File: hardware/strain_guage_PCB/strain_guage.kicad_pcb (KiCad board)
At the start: 4 copper layers, 132.7 x 89.5 mm, 97 parts, among them IC1 STM32C091CBT6, J2 Conn_02x05_Odd_Even, J3 Screw_Terminal_01x03, SW1 SW_Push, U1 MCP3561-E/ST, U10 MCP2221A-I/SL, U11 LM2664M6X/NOPB, U2 OP177GPZ, U3 OP177GPZ, U4 OP177GPZ, U5 AD630ARZ, U6 OPA2187IDR, U7 OP177GPZ, U8 AD9833BRMZ, U9 MIC5365-3.3YC5-TR

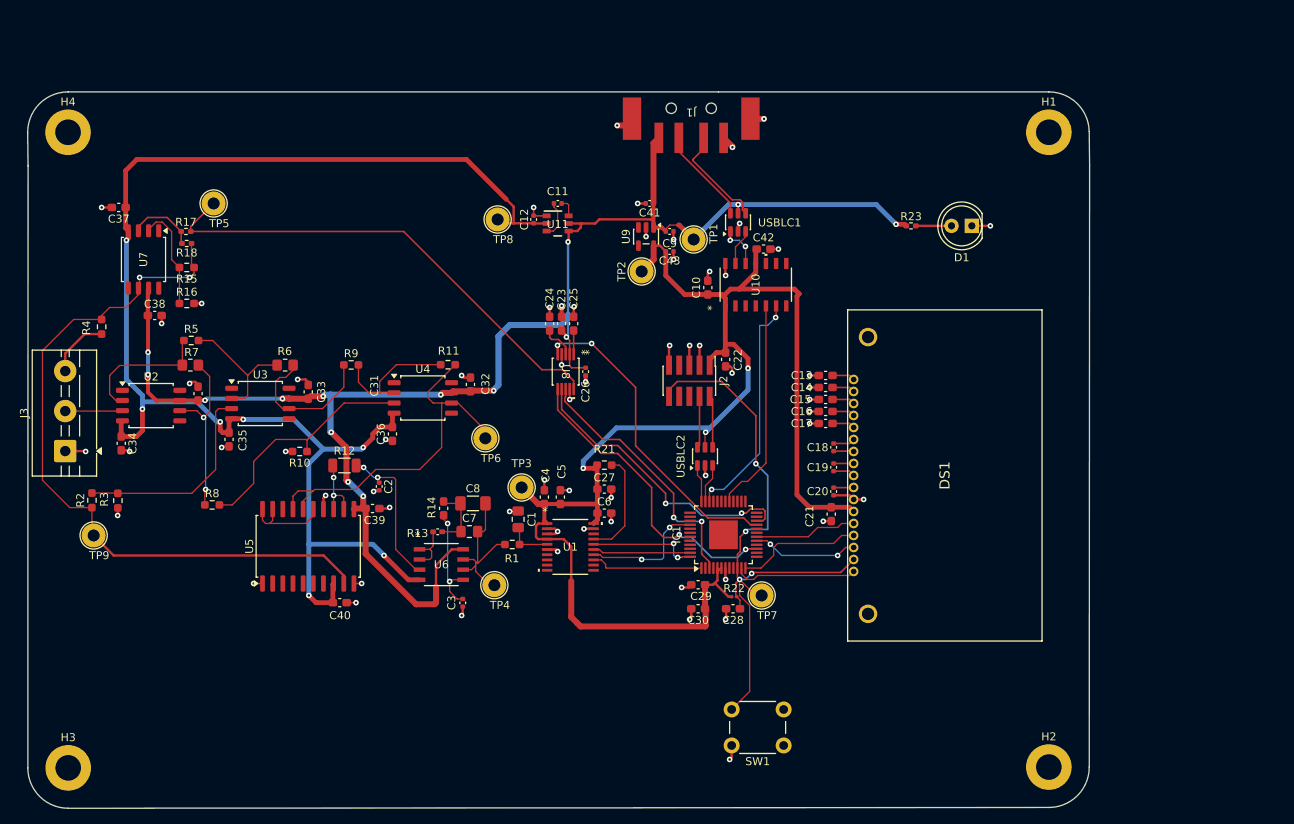
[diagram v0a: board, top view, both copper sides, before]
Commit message: PCB Revision + BOM Update
Footprints for Op-Amps were corrected, package size for R22 was updated. PCB Layout and Tracing marginally modified
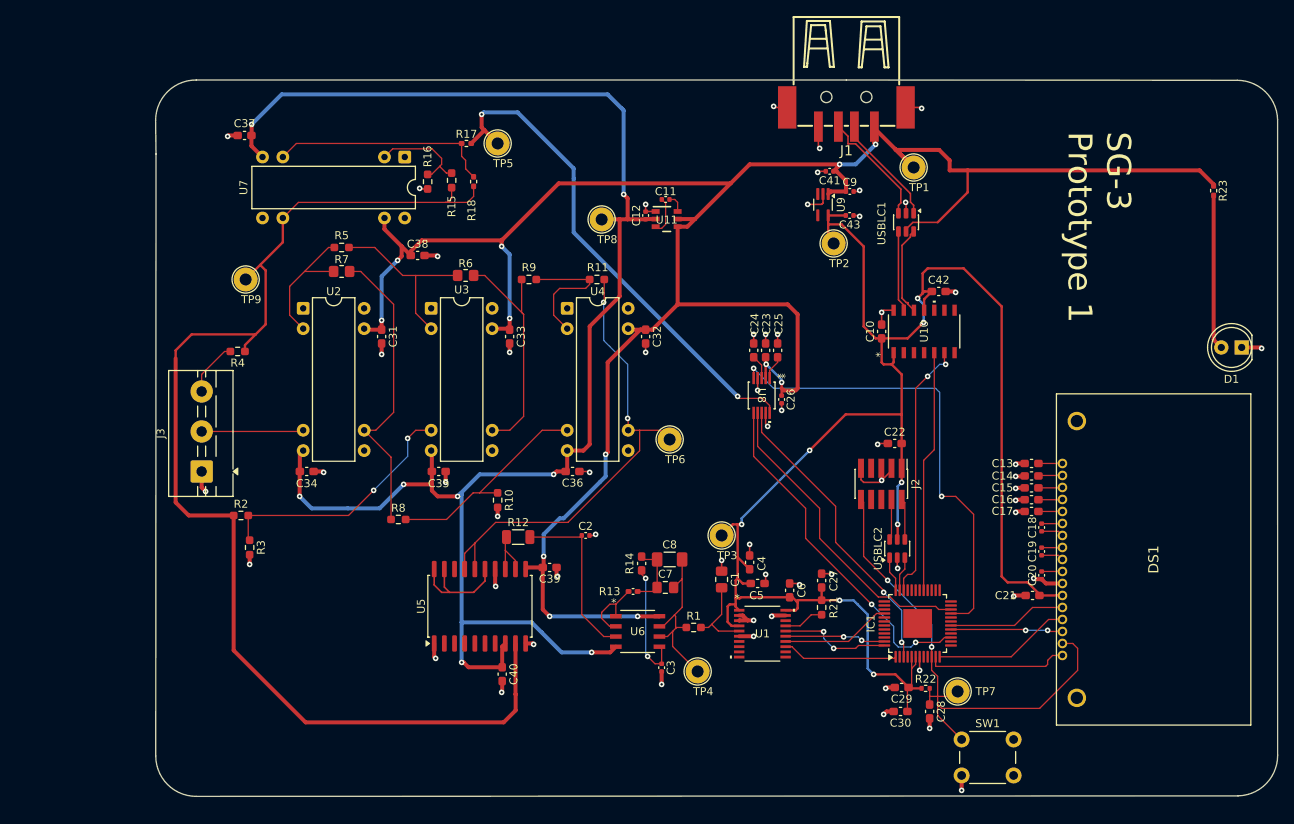
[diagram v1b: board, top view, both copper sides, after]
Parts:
- removed H1, H2, H3, H4: MountingHole_Pad, MountingHole:MountingHole_3.2mm_M3_ISO7380_Pad
- J1: footprint USBC:BX-TYPE-A-MWT4P -> USBC:USB-A-SMD_BX-TYPE-A-MWT4P
- R22: footprint Resistor_SMD:R_0201_0603Metric -> Resistor_SMD:R_0402_1005Metric
- U2, U3, U4, U7: footprint Package_SO:SOIC-8_5.3x5.3mm_P1.27mm -> Package_DIP:DIP-8-16_W7.62mm
- U9: footprint Package_TO_SOT_SMD:TSOT-23-5 -> Package_TO_SOT_SMD:SOT-353_SC-70-5_Handsoldering
- moved R23 38.1 mm to (214.5, 64.9), turned to -90 degrees
- moved TP9 37.2 mm to (93.5, 76.0)
- moved D1 37.0 mm to (218.0, 84.5)
- moved R17 36.7 mm to (121.1, 59.0)
- moved R18 36.7 mm to (122.0, 63.8), turned to 90 degrees
- moved TP5 36.3 mm to (125.0, 59.0)
- moved U7 35.1 mm to (113.4, 60.7)
- moved R15 34.9 mm to (119.2, 63.6), turned to 90 degrees
- moved R16 33.7 mm to (116.2, 63.8), turned to -90 degrees
- moved C38 33.7 mm to (115.0, 73.0)
- moved R21 32.5 mm to (165.5, 117.0), turned to 90 degrees
- moved C27 29.5 mm to (165.5, 113.6), turned to 90 degrees
- moved SW1 29.0 mm to (189.5, 138.0)
- moved TP1 28.9 mm to (177.0, 62.0), turned to 0 degrees
- moved C29 28.5 mm to (175.5, 127.0)
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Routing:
- net +5V: track 201.3 -> 293.8 mm, vias 14 -> 12
- net /C_EXC: track 90.0 -> 152.9 mm, vias 2 -> 0
- net +3V3: track 180.0 -> 218.2 mm, vias 3 -> 8
- net -5V: track 178.8 -> 208.0 mm, vias 7 -> 8
- net Net-(R17-Pad1): track 8.60 -> 27.8 mm
- net /FG_MCLK: track 39.8 -> 58.7 mm
- net Net-(R7-Pad1): track 21.8 -> 37.9 mm, vias 2 -> 0
- net Net-(D1-A): track 4.46 -> 19.4 mm
- net /ina_out: track 46.5 -> 60.8 mm, vias 0 -> 2
- net /NRST: track 78.7 -> 65.6 mm, vias 4 -> 2
- net Net-(R6-Pad1): track 18.7 -> 30.1 mm
- net Net-(U1-*IRQ/MDAT): track 13.4 -> 5.07 mm
- net /USBD-: track 17.6 -> 25.1 mm, vias 2 -> 0
- net /USBD+: track 18.5 -> 24.9 mm
- net Net-(R5-Pad1): track 16.8 -> 22.5 mm
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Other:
- board size 132.7 x 89.5 mm -> 140.3 x 89.5 mm
- board text added: "SG-3 Prototype 1"
